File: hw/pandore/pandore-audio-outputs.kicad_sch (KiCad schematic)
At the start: 2 parts, among them J12 TRS, J7 TRS

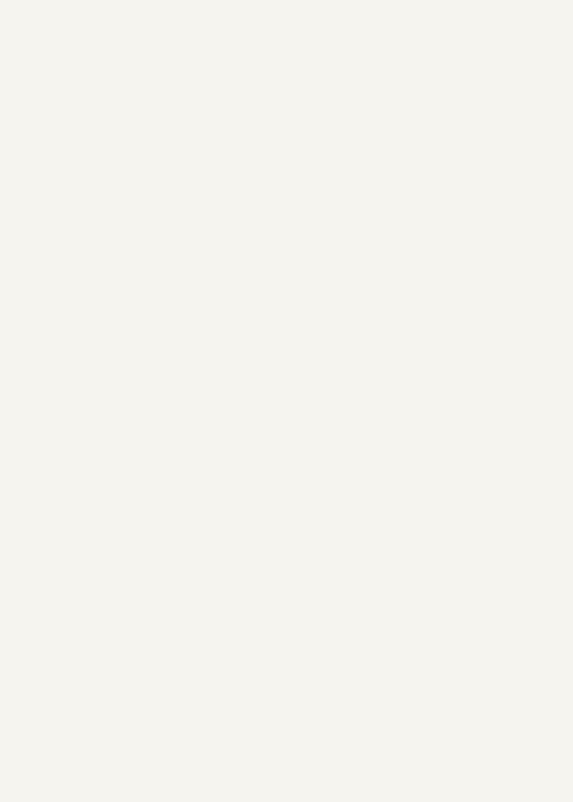
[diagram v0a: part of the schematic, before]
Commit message: Added lots to sch and pcb: eth passive, audio codec, midi, teensy Corrected and added support for M.2
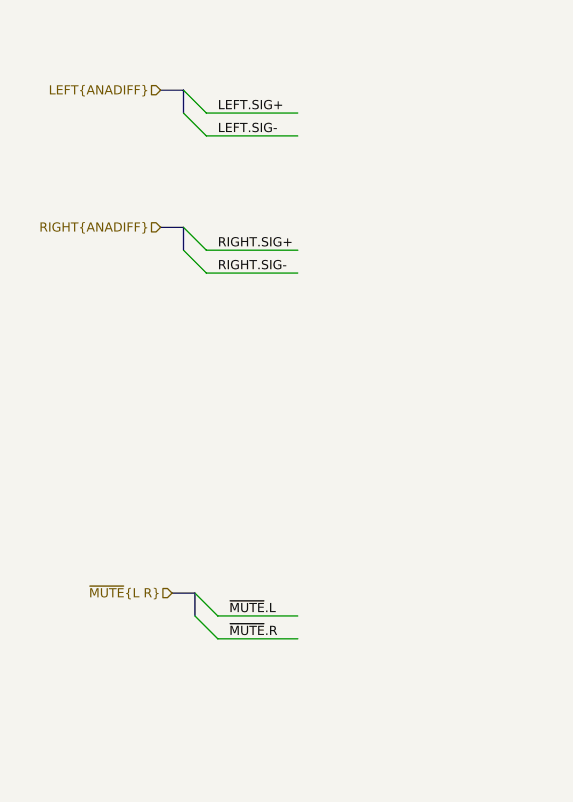
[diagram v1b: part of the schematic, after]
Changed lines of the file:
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@@
 		(company "${corp}")
+	)
+	(bus_entry
+		(at 53.34 91.44)
+		(size 2.54 2.54)
+		(stroke
+			(width 0)
+			(type default)
+		)
+	)
+	(bus_entry
+		(at 52.07 35.56)
+		(size 2.54 2.54)
+		(stroke
+			(width 0)
+			(type default)
+		)
+	)
+	(bus_entry
+		(at 52.07 48.26)
+		(size 2.54 2.54)
+		(stroke
+			(width 0)
+			(type default)
+		)
+	)
+	(bus_entry
+		(at 53.34 88.9)
+		(size 2.54 2.54)
+		(stroke
+			(width 0)
+			(type default)
+		)
+	)
+	(bus_entry
+		(at 52.07 50.8)
+		(size 2.54 2.54)
+		(stroke
+			(width 0)
+			(type default)
+		)
+	)
+	(bus_entry
+		(at 52.07 33.02)
+		(size 2.54 2.54)
+		(stroke
+			(width 0)
+			(type default)
+		)
+	)
+	(wire
+		(pts
+			(xy 55.88 93.98) (xy 64.77 93.98)
+		)
+		(stroke
+			(width 0)
+			(type default)
+		)
+	)
+	(bus
+		(pts
+			(xy 50.8 88.9) (xy 53.34 88.9)
+		)
+		(stroke
+			(width 0)
+			(type default)
+		)
+	)
+	(wire
+		(pts
+			(xy 54.61 50.8) (xy 64.77 50.8)
+		)
+		(stroke
+			(width 0)
+			(type default)
+		)
+	)
+	(bus
+		(pts
+			(xy 53.34 88.9) (xy 53.34 91.44)
+		)
+		(stroke
+			(width 0)
+			(type default)
+		)
+	)
+	(bus
+		(pts
+			(xy 49.53 48.26) (xy 52.07 48.26)
+		)
+		(stroke
+			(width 0)
+			(type default)
+		)
+	)
+	(bus
+		(pts
+			(xy 49.53 33.02) (xy 52.07 33.02)
+		)
+		(stroke
+			(width 0)
+			(type default)
+		)
+	)
+	(wire
+		(pts
+			(xy 54.61 35.56) (xy 64.77 35.56)
+		)
+		(stroke
+			(width 0)
+			(type default)
+		)
+	)
+	(wire
+		(pts
+			(xy 54.61 38.1) (xy 64.77 38.1)
+		)
+		(stroke
+			(width 0)
+			(type default)
+		)
+	)
+	(bus
+		(pts
+			(xy 52.07 48.26) (xy 52.07 50.8)
+		)
+		(stroke
+			(width 0)
+			(type default)
+		)
+	)
+	(wire
+		(pts
+			(xy 55.88 91.44) (xy 64.77 91.44)
+		)
+		(stroke
+			(width 0)
+			(type default)
+		)
+	)
+	(bus
+		(pts
+			(xy 52.07 33.02) (xy 52.07 35.56)
+		)
+		(stroke
+			(width 0)
+			(type default)
+		)
+	)
+	(wire
+		(pts
+			(xy 54.61 53.34) (xy 64.77 53.34)
+		)
+		(stroke
+			(width 0)
+			(type default)
+		)
+	)
+	(label "~{MUTE}.R"
+		(at 57.15 93.98 0)
+		(effects
+			(font
+				(size 1.016 1.016)
+			)
+			(justify left bottom)
+		)
+	)
+	(label "LEFT.SIG-"
+		(at 55.88 38.1 0)
+		(effects
+			(font
+				(size 1.016 1.016)
+			)
+			(justify left bottom)
+		)
+	)
+	(label "LEFT.SIG+"
+		(at 55.88 35.56 0)
+		(effects
+			(font
+				(size 1.016 1.016)
+			)
+			(justify left bottom)
+		)
+	)
+	(label "~{MUTE}.L"
+		(at 57.15 91.44 0)
+		(effects
+			(font
+				(size 1.016 1.016)
+			)
+			(justify left bottom)
+		)
+	)
+	(label "RIGHT.SIG+"
+		(at 55.88 50.8 0)
+		(effects
+			(font
+				(size 1.016 1.016)
+			)
+			(justify left bottom)
+		)
+	)
+	(label "RIGHT.SIG-"
+		(at 55.88 53.34 0)
+		(effects
+			(font
+				(size 1.016 1.016)
+			)
+			(justify left bottom)
+		)
+	)
+	(hierarchical_label "LEFT{ANADIFF}"
+		(shape input)
+		(at 49.53 33.02 180)
+		(effects
+			(font
+				(size 1.016 1.016)
+			)
+			(justify right)
+		)
+	)
+	(hierarchical_label "RIGHT{ANADIFF}"
+		(shape input)
+		(at 49.53 48.26 180)
+		(effects
+			(font
+				(size 1.016 1.016)
+			)
+			(justify right)
+		)
+	)
+	(hierarchical_label "~{MUTE}{L R}"
+		(shape input)
+		(at 50.8 88.9 180)
+		(effects
+			(font
+				(size 1.016 1.016)
+			)
+			(justify right)
+		)
 	)
 	(symbol

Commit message: lots of work done all around
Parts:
- added C122, C127, C137, C138: ${Capacitance}, ${Voltage}, ${Tolerance}, reekilib_cap:CAPAE630Xxxx, symbol reekilib_cap:cap_pol
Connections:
- net AVSS: now reaches J12.G
- net AVSS: now also J12.G, J12.TB, J12.TT
- net OUTR.SIG-: now reaches J12.RT
- net OUTR.SIG-: now also C138.2 (-)
- net OUTR.SIG+: now reaches J12.ST
- net OUTR.SIG+: now also C137.2 (-)
- net OUTL.SIG-: now reaches J12.RB
- net OUTL.SIG-: now also C127.2 (-)
- net OUTL.SIG+: now reaches J12.SB
- net OUTL.SIG+: now also C122.2 (-)
- new net OUT buffer L/OUT+: C122.1 (+)
- new net OUT buffer L/OUT-: C127.1 (+)
- new net OUT buffer R/OUT+: C137.1 (+)
- new net OUT buffer R/OUT-: C138.1 (+)
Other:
- added sheet OUT buffer L (pandore-audio-outbuf.kicad_sch)
- added sheet OUT buffer R (pandore-audio-outbuf.kicad_sch)
- moved on the sheet: J12A, J12B

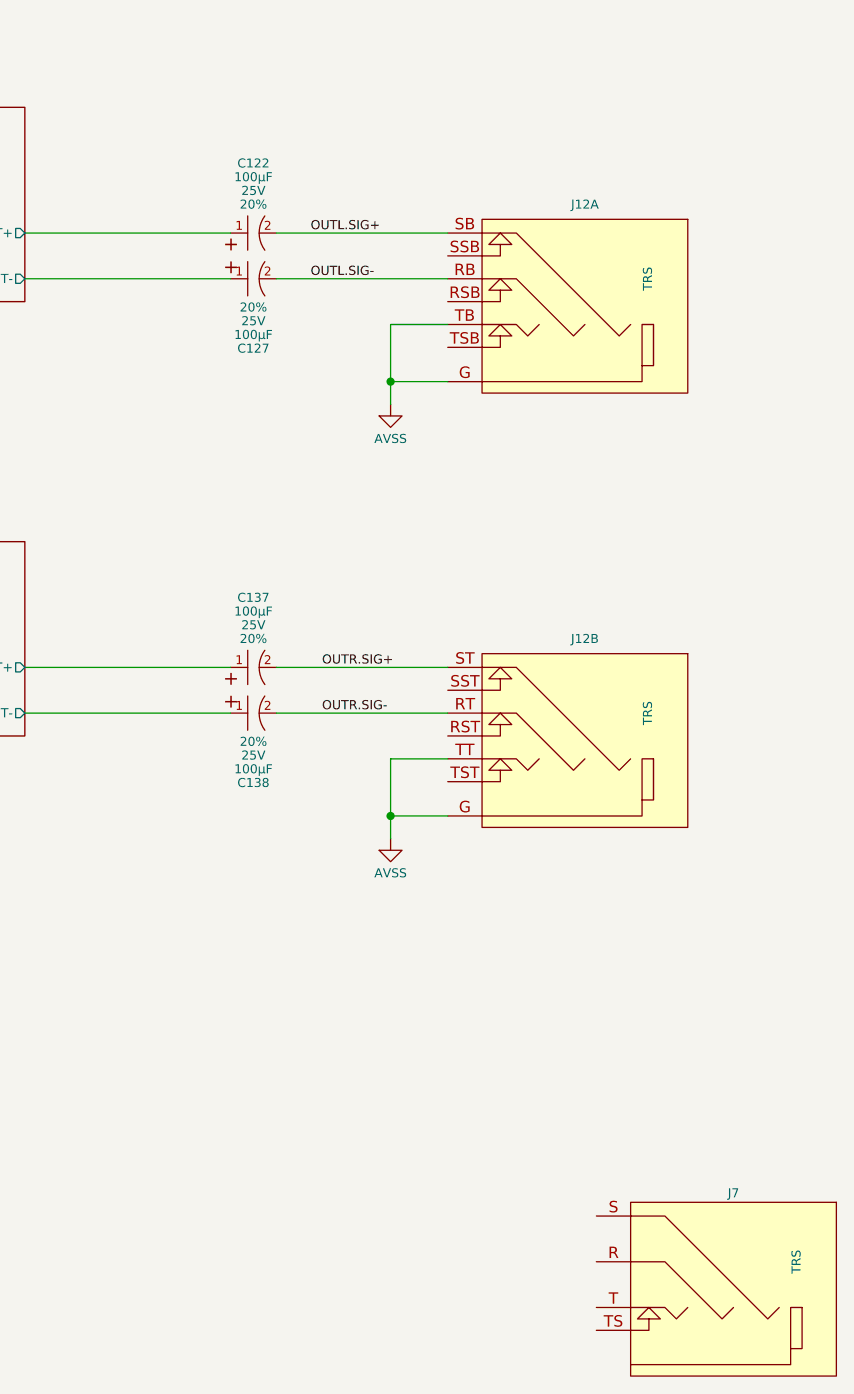
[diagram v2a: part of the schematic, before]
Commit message: added expansion port and more ctl to rp2350s routing much progress
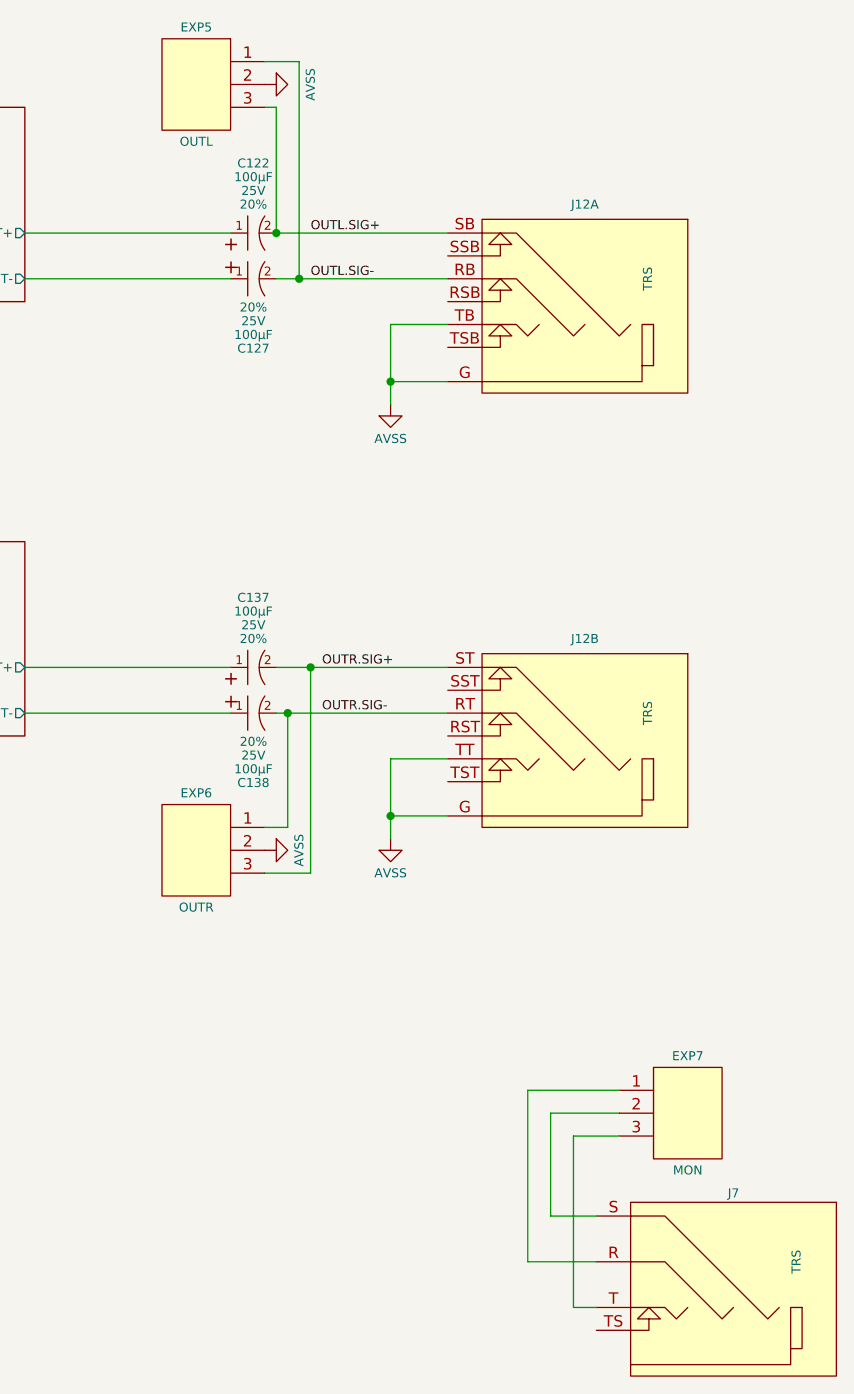
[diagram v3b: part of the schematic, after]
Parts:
- added EXP5: OUTL, reekilib_con:HDR254P1X03-TH, symbol reekilib_con:hdr-1x3
- added EXP6: OUTR, reekilib_con:HDR254P1X03-TH, symbol reekilib_con:hdr-1x3
- added EXP7: MON, reekilib_con:HDR254P1X03-TH, symbol reekilib_con:hdr-1x3
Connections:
- net AVSS: now also EXP5.2, EXP6.2
- net OUTL.SIG+: now also EXP5.3
- net OUTL.SIG-: now also EXP5.1
- net OUTR.SIG+: now also EXP6.3
- net OUTR.SIG-: now also EXP6.1
- net at J7.R: now also EXP7.1
- net at J7.S: now also EXP7.2
- net at J7.T: now also EXP7.3

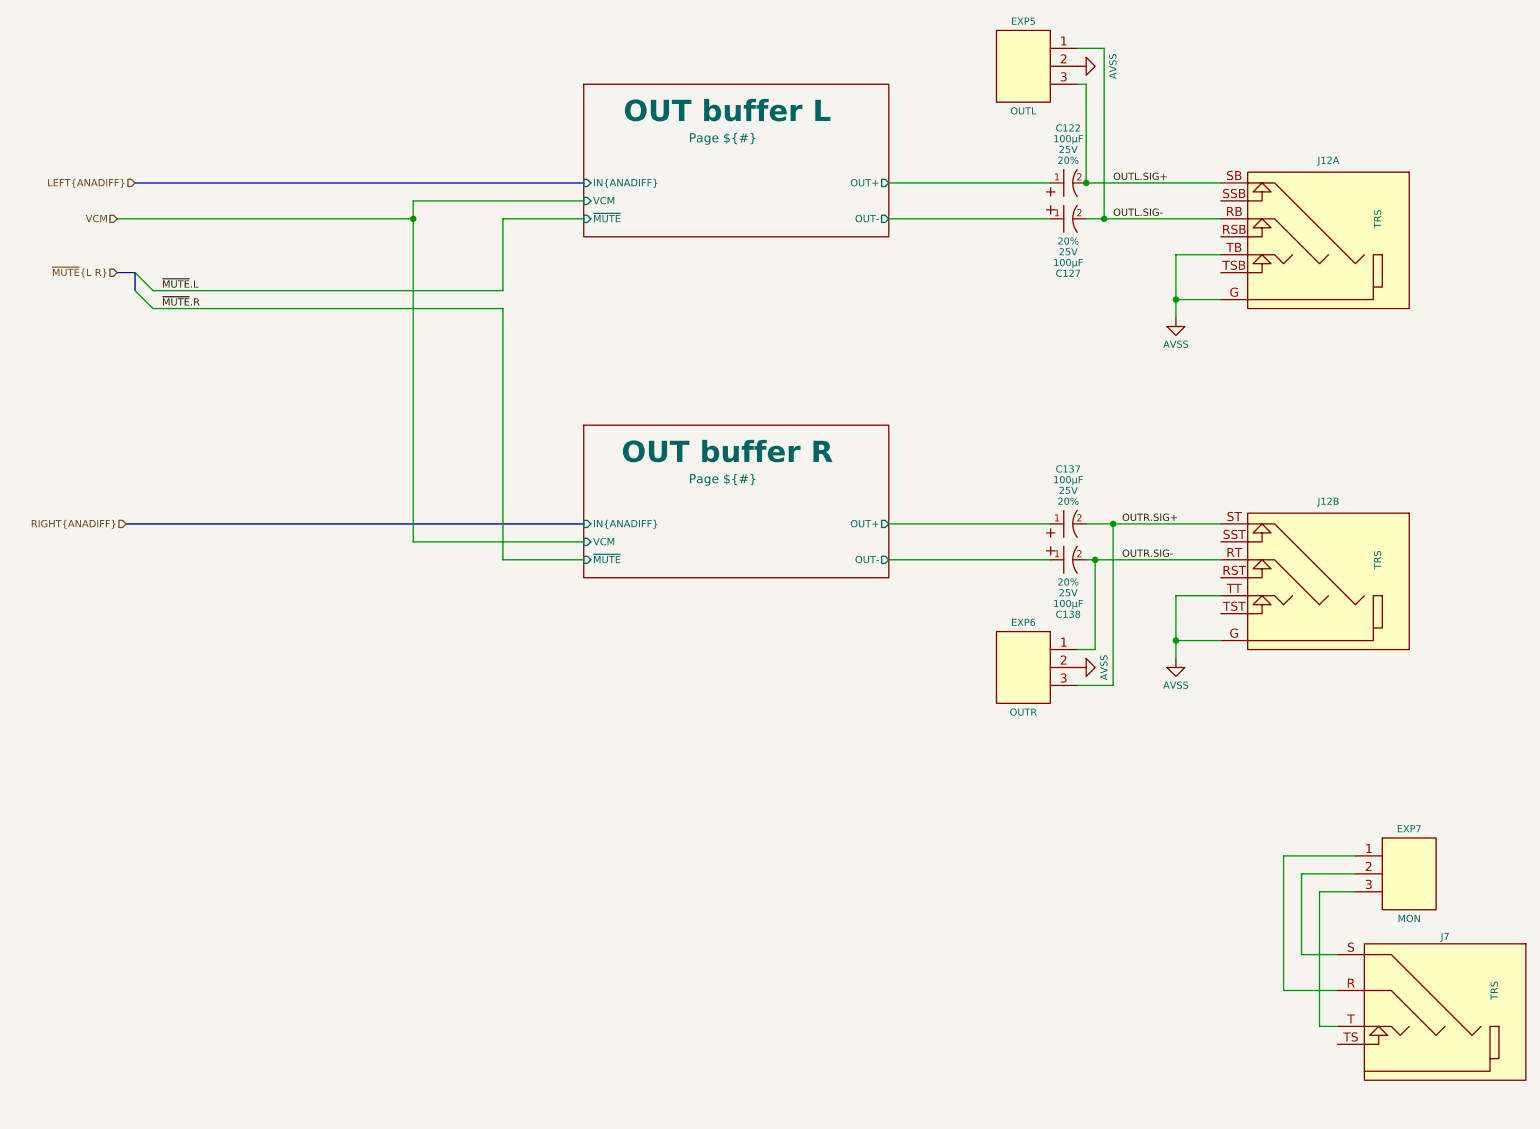
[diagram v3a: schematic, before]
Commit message: added monitor amp with volume knob continue routing all around
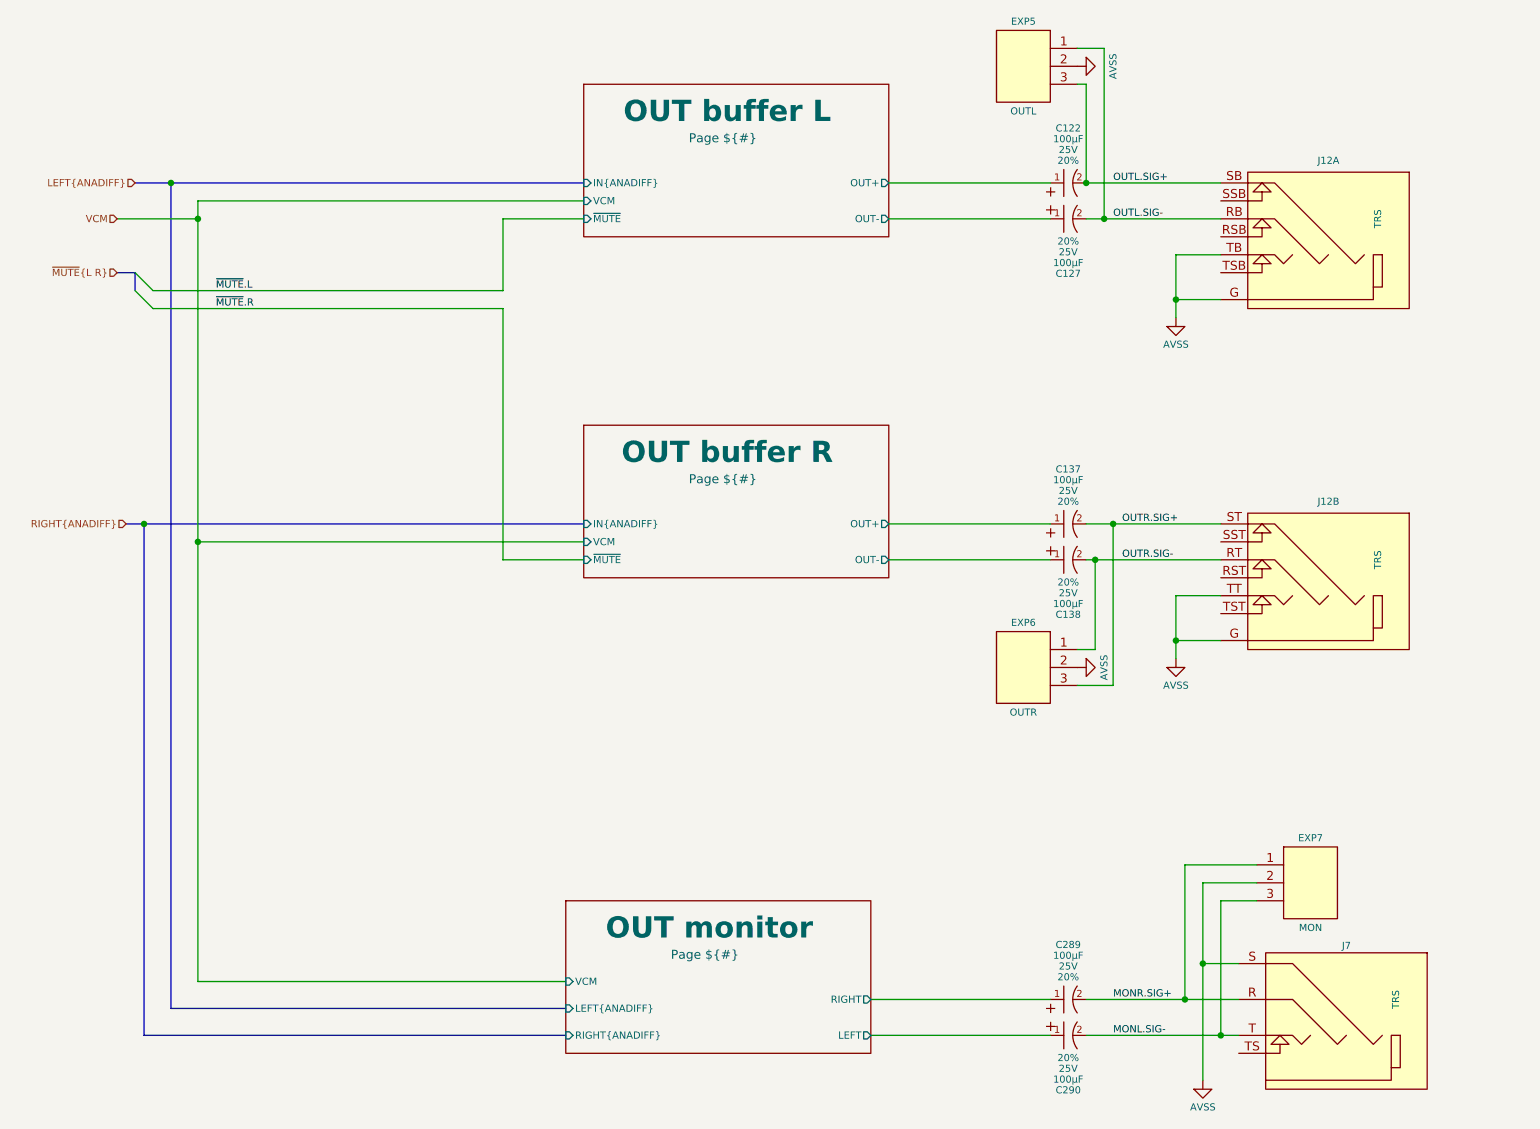
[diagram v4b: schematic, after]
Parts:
- added C289, C290: ${Capacitance}, ${Voltage}, ${Tolerance}, reekilib_cap:CAPAE630Xxxx, symbol reekilib_cap:cap_pol
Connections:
- net AVSS: now also EXP7.2, J7.S
- net MONR.SIG+: now reaches EXP7.1, J7.R
- net MONR.SIG+: now also C289.2 (-)
- net MONL.SIG-: now reaches EXP7.3, J7.T
- net MONL.SIG-: now also C290.2 (-)
- new net OUT monitor/LEFT: C290.1 (+)
- new net OUT monitor/RIGHT: C289.1 (+)
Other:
- added sheet OUT monitor (pandore-audio-monitor.kicad_sch)
- moved on the sheet: EXP7, J7

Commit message: last sprint almost done, most routing done
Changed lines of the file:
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@@
-	)
-	(junction
-		(at 58.42 92.71)
-		(diameter 0)
-		(color 0 0 0 0)
 	)
 	(junction
@@
 	(wire
 		(pts
+			(xy 46.99 154.94) (xy 110.49 154.94)
+		)
+		(stroke
+			(width 0)
+			(type default)
+		)
+	)
+	(wire
+		(pts
 			(xy 187.96 90.17) (xy 203.2 90.17)
 		)
@@
 	(wire
 		(pts
-			(xy 110.49 154.94) (xy 58.42 154.94)
-		)
-		(stroke
-			(width 0)
-			(type default)
-		)
-	)
-	(wire
-		(pts
 			(xy 46.99 46.99) (xy 58.42 46.99)
 		)
@@
 		(pts
 			(xy 187.96 90.17) (xy 187.96 113.03)
-		)
-		(stroke
-			(width 0)
-			(type default)
-		)
-	)
-	(wire
-		(pts
-			(xy 58.42 92.71) (xy 58.42 154.94)
 		)
 		(stroke
@@
 		(effects
 			(font
+				(size 1.016 1.016)
+			)
+			(justify right)
+		)
+	)
+	(hierarchical_label "VCMMON"
+		(shape input)
+		(at 46.99 154.94 180)
+		(effects
+			(font

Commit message: finished adding mpn,mfg to all parts, finished routing placement
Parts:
- EXP5, EXP6, EXP7: Link url-link -> (none); MFG MFG -> Adam Tech; MPN MPN -> PH1-03-UA
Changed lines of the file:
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@@
 			)
 		)
-		(property "Datasheet" "url-ds"
+		(property "Datasheet" "https://app.adam-tech.com/products/download/data_sheet/201605/ph1-xx-ua-data-sheet.pdf"
 			(at 175.26 124.206 0)
 			(do_not_autoplace yes)
@@
 			)
 		)
-		(property "Link" "url-link"
+		(property "Link" ""
 			(at 175.26 122.936 0)
 			(do_not_autoplace yes)
@@
 			)
 		)
-		(property "MPN" "MPN"
+		(property "MPN" "PH1-03-UA"
 			(at 175.26 118.364 0)
 			(do_not_autoplace yes)
@@
 			)
 		)
-		(property "MFG" "MFG"
+		(property "MFG" "Adam Tech"
 			(at 168.656 118.364 0)
 			(do_not_autoplace yes)
@@
 			)
 		)
-		(property "Datasheet" "url-ds"
+		(property "Datasheet" "https://app.adam-tech.com/products/download/data_sheet/201605/ph1-xx-ua-data-sheet.pdf"
 			(at 175.26 39.116 0)
 			(do_not_autoplace yes)
@@
 			)
 		)
-		(property "Link" "url-link"
+		(property "Link" ""
 			(at 175.26 37.846 0)
 			(do_not_autoplace yes)
@@
 			)
 		)
-		(property "MPN" "MPN"
+		(property "MPN" "PH1-03-UA"
 			(at 175.26 33.274 0)
 			(do_not_autoplace yes)
@@
 			)
 		)
-		(property "MFG" "MFG"
+		(property "MFG" "Adam Tech"
 			(at 168.656 33.274 0)
 			(do_not_autoplace yes)
@@
 			)
 		)
-		(property "Datasheet" "url-ds"
+		(property "Datasheet" "https://app.adam-tech.com/products/download/data_sheet/201605/ph1-xx-ua-data-sheet.pdf"
 			(at 215.9 154.686 0)
 			(do_not_autoplace yes)
@@
 			)
 		)
-		(property "Link" "url-link"
+		(property "Link" ""
 			(at 215.9 153.416 0)
 			(do_not_autoplace yes)
@@
 			)
 		)
-		(property "MPN" "MPN"
+		(property "MPN" "PH1-03-UA"
 			(at 215.9 148.844 0)
 			(do_not_autoplace yes)
@@
 			)
 		)
-		(property "MFG" "MFG"
+		(property "MFG" "Adam Tech"
 			(at 222.504 148.844 0)
 			(do_not_autoplace yes)
